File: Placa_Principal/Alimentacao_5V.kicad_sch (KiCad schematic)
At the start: 6 parts, among them J1 Conn_01x02, Q2 IRF9540N, SW1 MTS102-C4, U3 DSN-MINI-360 SCH

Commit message: Segundo commit
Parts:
- D1: footprint LED_THT:LED_D4.0mm -> LED_THT:LED_D10.0mm
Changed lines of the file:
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@@
 			)
 		)
-		(property "Footprint" "LED_THT:LED_D4.0mm"
+		(property "Footprint" "LED_THT:LED_D10.0mm"
 			(at 201.93 92.71 0)
 			(effects

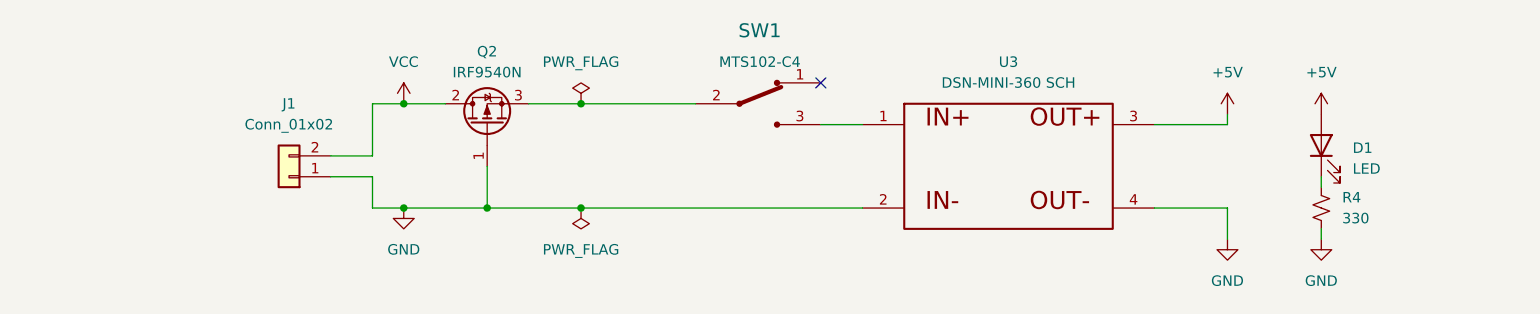
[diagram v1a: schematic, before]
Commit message: Finalizando o esquemático e rearranjando a posição dos componentes na PCB
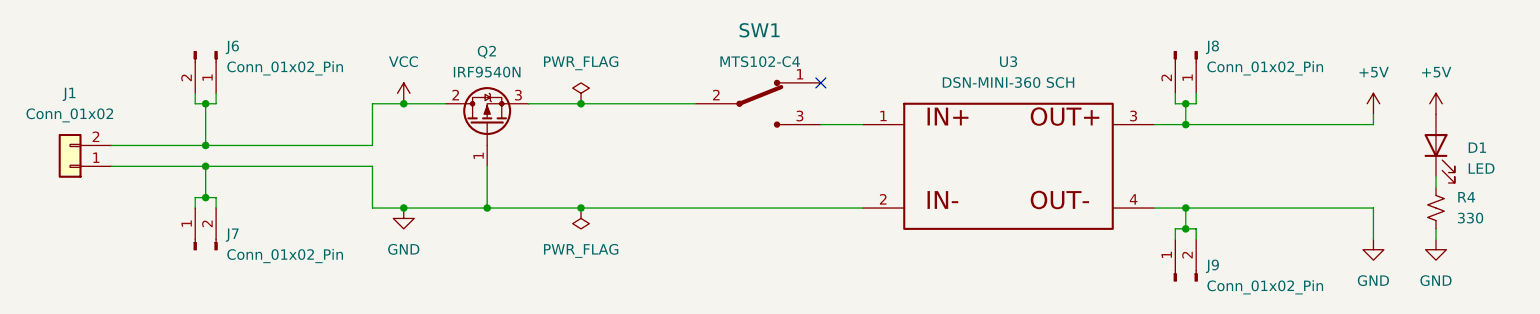
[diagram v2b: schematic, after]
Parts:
- added J6, J7, J8, J9: Conn_01x02_Pin, Connector_PinHeader_2.54mm:PinHeader_1x02_P2.54mm_Vertical, symbol Connector:Conn_01x02_Pin
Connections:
- net +5V: now also J8.1 (Pin_1), J8.2 (Pin_2)
- net GND: now also J7.1 (Pin_1), J7.2 (Pin_2), J9.1 (Pin_1), J9.2 (Pin_2)
- net VCC: now also J6.1 (Pin_1), J6.2 (Pin_2)
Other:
- moved on the sheet: D1, J1, R4

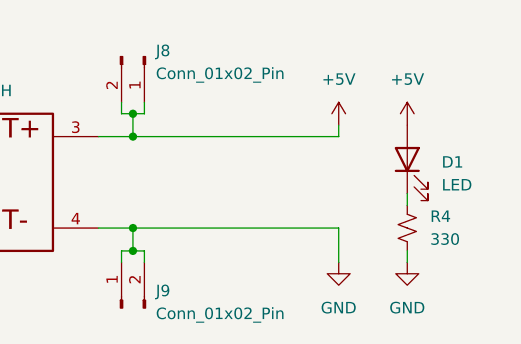
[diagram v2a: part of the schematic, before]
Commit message: Atualizando a alimentação de todos os sensores e ESP para 3.3V e finalizando o design do monitoramento da bateria e feedback geral
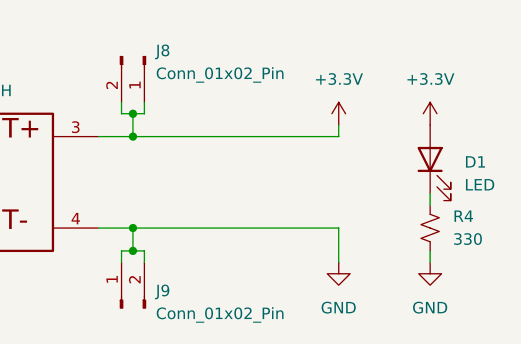
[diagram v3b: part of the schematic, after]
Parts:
- Q2: footprint Package_TO_SOT_THT:TO-220-3_Horizontal_TabDown -> Package_TO_SOT_THT:TO-220-3_Vertical
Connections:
- net +5V renamed +3.3V
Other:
- moved on the sheet: D1, R4
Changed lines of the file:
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@@
 	(wire
 		(pts
-			(xy 215.9 96.52) (xy 215.9 97.79)
+			(xy 218.44 96.52) (xy 218.44 97.79)
 		)
 		(stroke
@@
 	(wire
 		(pts
-			(xy 215.9 102.87) (xy 215.9 104.14)
+			(xy 218.44 102.87) (xy 218.44 104.14)
 		)
 		(stroke
@@
 	(symbol
 		(lib_id "power:GND")
-		(at 215.9 104.14 0)
+		(at 218.44 104.14 0)
 		(unit 1)
 		(exclude_from_sim no)
@@
 		(fields_autoplaced yes)
 		(property "Reference" "#PWR016"
-			(at 215.9 110.49 0)
+			(at 218.44 110.49 0)
 			(effects
 				(font
@@
 		)
 		(property "Value" "GND"
-			(at 215.9 109.22 0)
+			(at 218.44 109.22 0)
 			(effects
 				(font
@@
 		)
 		(property "Footprint" ""
-			(at 215.9 104.14 0)
+			(at 218.44 104.14 0)
 			(effects
 				(font
@@
 		)
 		(property "Datasheet" ""
-			(at 215.9 104.14 0)
+			(at 218.44 104.14 0)
 			(effects
 				(font
@@
 		)
 		(property "Description" "Power symbol creates a global label with name \"GND\" , ground"
-			(at 215.9 104.14 0)
+			(at 218.44 104.14 0)
 			(effects
 				(font
@@
 	)
 	(symbol
+		(lib_id "power:+3.3V")
+		(at 208.28 88.9 0)
+		(unit 1)
+		(exclude_from_sim no)
+		(in_bom yes)
+		(on_board yes)
+		(dnp no)
+		(fields_autoplaced yes)
+		(property "Reference" "#PWR05"
+			(at 208.28 92.71 0)
+			(effects
+				(font
+					(size 1.27 1.27)
+				)
+				(hide yes)
+			)
+		)
+		(property "Value" "+3.3V"
+			(at 208.28 83.82 0)
+			(effects
+				(font
+					(size 1.27 1.27)
+				)
+			)
+		)
+		(property "Footprint" ""
+			(at 208.28 88.9 0)
+			(effects
+				(font
+					(size 1.27 1.27)
+				)
+				(hide yes)
+			)
+		)
+		(property "Datasheet" ""
+			(at 208.28 88.9 0)
+			(effects
+				(font
+					(size 1.27 1.27)
+				)
+				(hide yes)
+			)
+		)
+		(property "Description" "Power symbol creates a global label with name \"+3.3V\""
+			(at 208.28 88.9 0)
+			(effects
+				(font
+					(size 1.27 1.27)
+				)
+				(hide yes)
+			)
+		)
+		(pin "1"
+		)
+		(instances
+			(project "Placa_Principal"
+				(path "/02649df7-f0d0-431b-8f11-0967d1dd03be/d787e3dc-0c72-4903-b069-be5f90fb6ecc"
+					(reference "#PWR05")
+					(unit 1)
+				)
+			)
+		)
+	)
+	(symbol
 		(lib_id "power:GND")
 		(at 208.28 104.14 0)
@@
 	)
 	(symbol
-		(lib_id "power:+5V")
-		(at 208.28 88.9 0)
-		(unit 1)
-		(exclude_from_sim no)
-		(in_bom yes)
-		(on_board yes)
-		(dnp no)
-		(fields_autoplaced yes)
-		(property "Reference" "#PWR09"
-			(at 208.28 92.71 0)
-			(effects
-				(font
-					(size 1.27 1.27)
-				)
-				(hide yes)
-			)
-		)
-		(property "Value" "+5V"
-			(at 208.28 83.82 0)
-			(effects
-				(font
-					(size 1.27 1.27)
-				)
-			)
-		)
-		(property "Footprint" ""
-			(at 208.28 88.9 0)
-			(effects
-				(font
-					(size 1.27 1.27)
-				)
-				(hide yes)
-			)
-		)
-		(property "Datasheet" ""
-			(at 208.28 88.9 0)
-			(effects
-				(font
-					(size 1.27 1.27)
-				)
-				(hide yes)
-			)
-		)
-		(property "Description" "Power symbol creates a global label with name \"+5V\""
-			(at 208.28 88.9 0)
-			(effects
-				(font
-					(size 1.27 1.27)
-				)
-				(hide yes)
-			)
-		)
-		(pin "1"
-		)
-		(instances
-			(project "Placa_Principal"
-				(path "/02649df7-f0d0-431b-8f11-0967d1dd03be/d787e3dc-0c72-4903-b069-be5f90fb6ecc"
-					(reference "#PWR09")
-					(unit 1)
-				)
-			)
-		)
-	)
-	(symbol
 		(lib_id "Connector:Conn_01x02_Pin")
 		(at 64.77 105.41 90)
@@
 	)
 	(symbol
+		(lib_id "power:+3.3V")
+		(at 218.44 88.9 0)
+		(unit 1)
+		(exclude_from_sim no)
+		(in_bom yes)
+		(on_board yes)
+		(dnp no)
+		(fields_autoplaced yes)
+		(property "Reference" "#PWR07"
+			(at 218.44 92.71 0)
+			(effects
+				(font
+					(size 1.27 1.27)
+				)
+				(hide yes)
+			)
+		)
+		(property "Value" "+3.3V"
+			(at 218.44 83.82 0)
+			(effects
+				(font
+					(size 1.27 1.27)
+				)
+			)
+		)
+		(property "Footprint" ""
+			(at 218.44 88.9 0)
+			(effects
+				(font
+					(size 1.27 1.27)
+				)
+				(hide yes)
+			)
+		)
+		(property "Datasheet" ""
+			(at 218.44 88.9 0)
+			(effects
+				(font
+					(size 1.27 1.27)
+				)
+				(hide yes)
+			)
+		)
+		(property "Description" "Power symbol creates a global label with name \"+3.3V\""
+			(at 218.44 88.9 0)
+			(effects
+				(font
+					(size 1.27 1.27)
+				)
+				(hide yes)
+			)
+		)
+		(pin "1"
+		)
+		(instances
+			(project "Placa_Principal"
+				(path "/02649df7-f0d0-431b-8f11-0967d1dd03be/d787e3dc-0c72-4903-b069-be5f90fb6ecc"
+					(reference "#PWR07")
+					(unit 1)
+				)
+			)
+		)
+	)
+	(symbol
 		(lib_id "power:VCC")
 		(at 90.17 87.63 0)
@@
 	)
 	(symbol
-		(lib_id "power:+5V")
-		(at 215.9 88.9 0)
-		(unit 1)
-		(exclude_from_sim no)
-		(in_bom yes)
-		(on_board yes)
-		(dnp no)
-		(fields_autoplaced yes)
-		(property "Reference" "#PWR015"
-			(at 215.9 92.71 0)
-			(effects
-				(font
-					(size 1.27 1.27)
-				)
-				(hide yes)
-			)
-		)
-		(property "Value" "+5V"
-			(at 215.9 83.82 0)
-			(effects
-				(font
-					(size 1.27 1.27)
-				)
-			)
-		)
-		(property "Footprint" ""
-			(at 215.9 88.9 0)
-			(effects
-				(font
-					(size 1.27 1.27)
-				)
-				(hide yes)
-			)
-		)
-		(property "Datasheet" ""
-			(at 215.9 88.9 0)
-			(effects
-				(font
-					(size 1.27 1.27)
-				)
-				(hide yes)
-			)
-		)
-		(property "Description" "Power symbol creates a global label with name \"+5V\""
-			(at 215.9 88.9 0)
-			(effects
-				(font
-					(size 1.27 1.27)
-				)
-				(hide yes)
-			)
-		)
-		(pin "1"
-		)
-		(instances
-			(project "Placa_Principal"
-				(path "/02649df7-f0d0-431b-8f11-0967d1dd03be/d787e3dc-0c72-4903-b069-be5f90fb6ecc"
-					(reference "#PWR015")
-					(unit 1)
-				)
-			)
-		)
-	)
-	(symbol
 		(lib_id "Device:R_Small_US")
-		(at 215.9 100.33 0)
+		(at 218.44 100.33 0)
 		(unit 1)
 		(exclude_from_sim no)
@@
 		(fields_autoplaced yes)
 		(property "Reference" "R4"
-			(at 218.44 99.0599 0)
+			(at 220.98 99.0599 0)
 			(effects
 				(font
@@
 		)
 		(property "Value" "330"
-			(at 218.44 101.5999 0)
+			(at 220.98 101.5999 0)
 			(effects
 				(font
@@
 		)
 		(property "Footprint" "Resistor_THT:R_Axial_DIN0204_L3.6mm_D1.6mm_P5.08mm_Horizontal"
-			(at 215.9 100.33 0)
+			(at 218.44 100.33 0)
 			(effects
 				(font
@@
 		)
 		(property "Datasheet" "~"
-			(at 215.9 100.33 0)
+			(at 218.44 100.33 0)
 			(effects
 				(font
@@
 		)
 		(property "Description" "Resistor, small US symbol"
-			(at 215.9 100.33 0)
+			(at 218.44 100.33 0)
 			(effects
 				(font
@@
 			)
 		)
-		(property "Footprint" "Package_TO_SOT_THT:TO-220-3_Horizontal_TabDown"
+		(property "Footprint" "Package_TO_SOT_THT:TO-220-3_Vertical"
 			(at 102.235 85.09 0)
 			(effects
@@
 	(symbol
 		(lib_id "Device:LED")
-		(at 215.9 92.71 90)
+		(at 218.44 92.71 90)
 		(unit 1)
 		(exclude_from_sim no)
@@
 		(fields_autoplaced yes)
 		(property "Reference" "D1"
-			(at 219.71 93.0274 90)
+			(at 222.25 93.0274 90)
 			(effects
 				(font
@@
 		)
 		(property "Value" "LED"
-			(at 219.71 95.5674 90)
+			(at 222.25 95.5674 90)
 			(effects
 				(font
@@
 		)
 		(property "Footprint" "LED_THT:LED_D10.0mm"
-			(at 215.9 92.71 0)
+			(at 218.44 92.71 0)
 			(effects
 				(font
@@
 		)
 		(property "Datasheet" "~"
-			(at 215.9 92.71 0)
+			(at 218.44 92.71 0)
 			(effects
 				(font
@@
 		)
 		(property "Description" "Light emitting diode"
-			(at 215.9 92.71 0)
+			(at 218.44 92.71 0)
 			(effects
 				(font
@@
 		)
 		(property "Sim.Pins" "1=K 2=A"
-			(at 215.9 92.71 0)
-			(effects
-				(font
+			(at 218.44 92.71 0)
+			(effects
+				(font
